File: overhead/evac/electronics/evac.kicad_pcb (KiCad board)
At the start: 2 copper layers, 145 x 47.3 mm, 39 parts, among them J1 Conn_02x01, J2 Conn_02x01, J3 Conn_02x03_Counter_Clockwise, J4 Conn_02x01

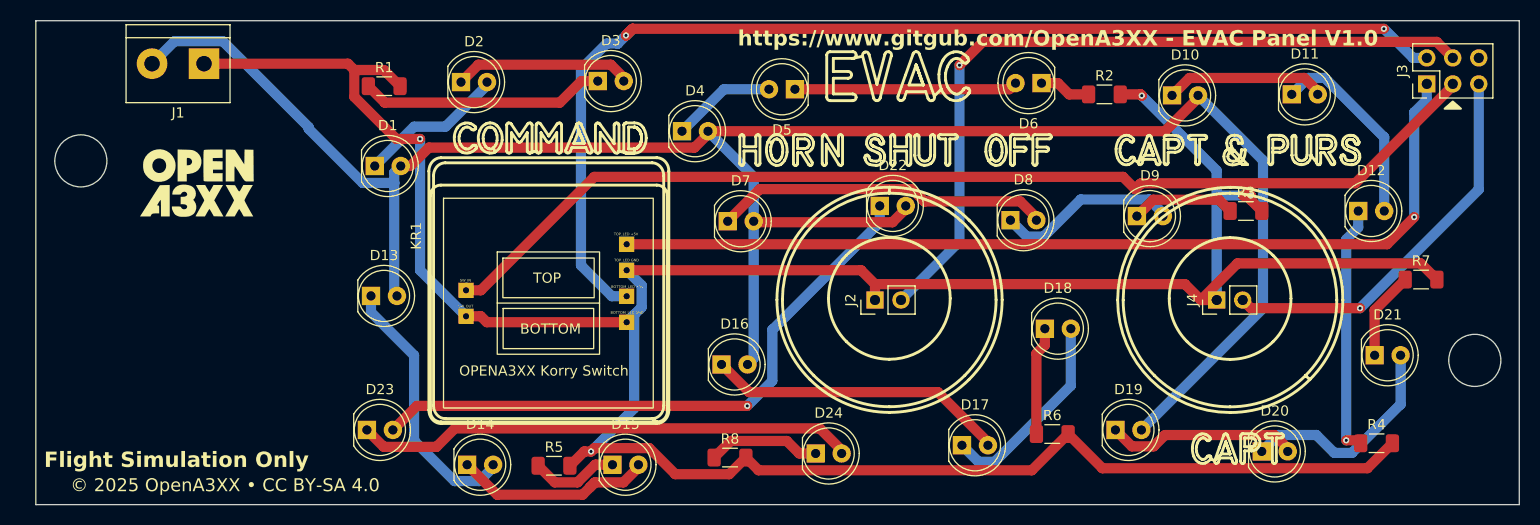
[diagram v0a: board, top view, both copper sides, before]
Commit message: Updated all LEDs for SMD!
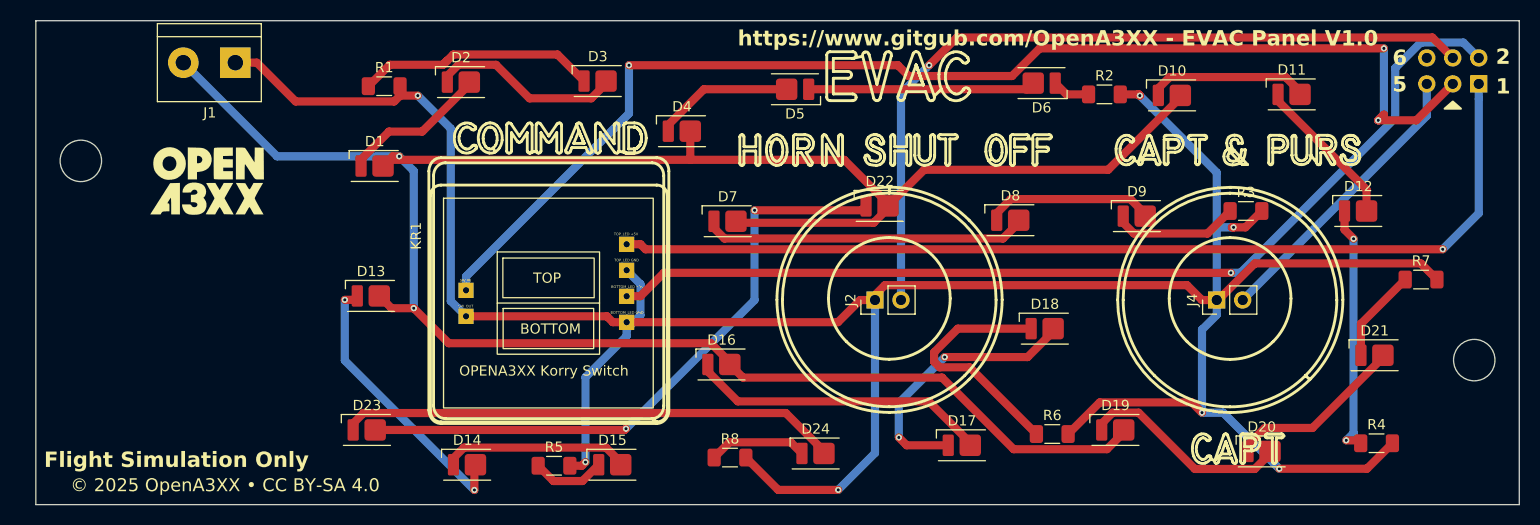
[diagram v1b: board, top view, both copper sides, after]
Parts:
- D1, D10, D11, D12, D13, D14, D15, D16, D17, D18, D19, D2, D20, D21, D22, D23, D24, D3, D4, D5, D6, D7, D8, D9: footprint LED_THT:LED_D5.0mm_Clear -> OpenA3XX:LED_Everlight-SMD3528_3.5x2.8mm_67-21ST
- J3: moved to B.Cu
- moved J3 5.08 mm to (213.6, 84.7)
- moved J1 3.06 mm to (92.1, 82.6)
- moved bottom 1.02 mm to (89.6, 94.1)
- moved top 1.02 mm to (89.4, 94.1)
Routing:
- net +12V: track 205.5 -> 225.6 mm, vias 0 -> 2
- net Net-(J3-Pin_2): track 114.1 -> 97.0 mm, vias 2 -> 1
- net Net-(J3-Pin_3): track 106.6 -> 123.1 mm, vias 0 -> 3
- net GND: track 294.3 -> 278.0 mm, vias 4 -> 7
- net Net-(D18-K): track 10.6 -> 24.3 mm
- net Net-(J3-Pin_5): track 38.5 -> 28.6 mm, vias 1 -> 0
- net Net-(D17-K): track 20.0 -> 26.8 mm, vias 0 -> 2
- net Net-(J3-Pin_1): track 91.6 -> 97.6 mm
- net Net-(D11-K): track 19.3 -> 15.0 mm
- net Net-(D20-K): track 21.7 -> 17.6 mm
- net Net-(D4-K): track 10.2 -> 13.6 mm
- net Net-(D9-K): track 10.2 -> 12.4 mm
- net Net-(J2-Pin_2): track 75.1 -> 77.2 mm
- net Net-(D19-K): track 18.8 -> 20.6 mm
- net Net-(D14-K): track 20.0 -> 18.3 mm
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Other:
- outline, holes or cut-outs redrawn
- board text added: "1"
- board text added: "2"
- board text added: "5"
- board text added: "6"

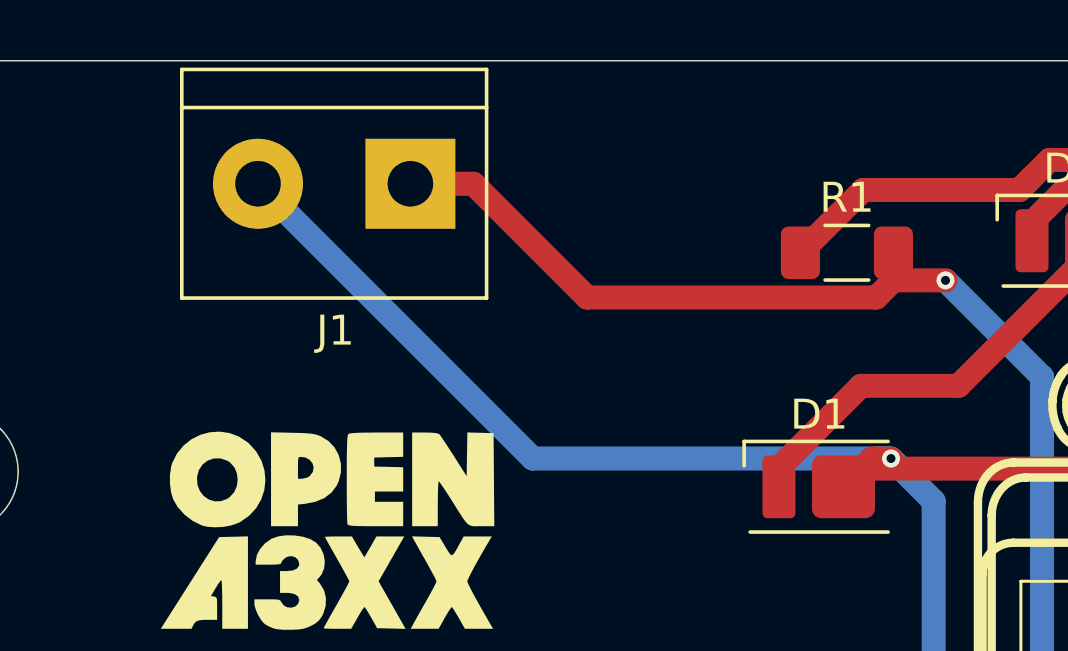
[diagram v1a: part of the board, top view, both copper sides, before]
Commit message: Added terminal connector to 3D models
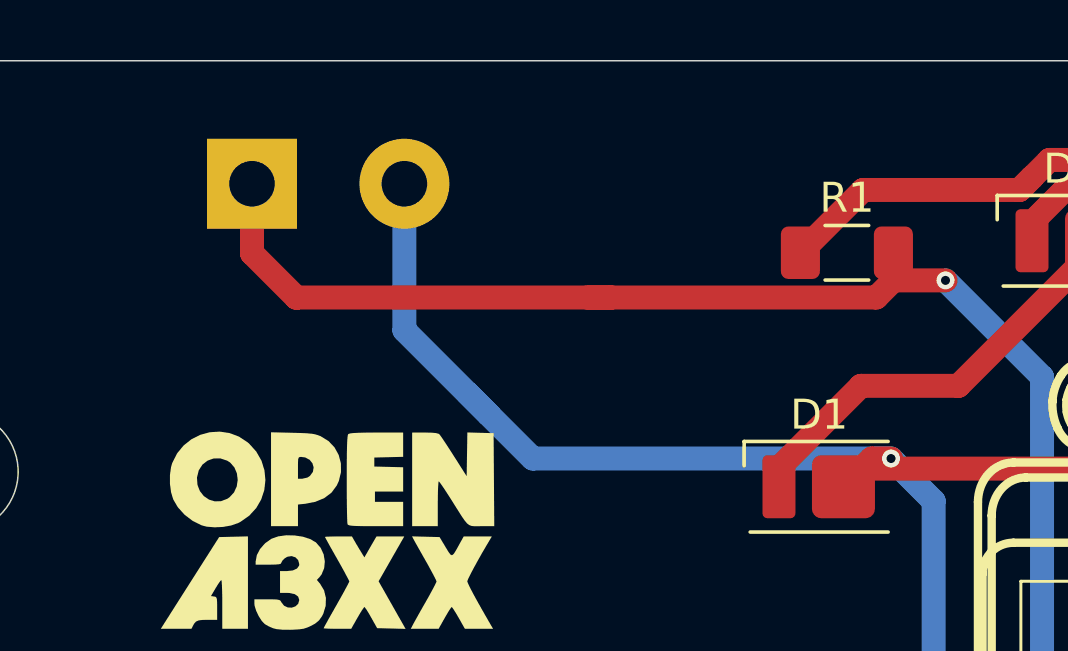
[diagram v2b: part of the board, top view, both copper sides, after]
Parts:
- J1: moved to B.Cu
- moved J1 5.28 mm to (86.8, 82.6), turned to 0 degrees
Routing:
- net GND: track 278.0 -> 285.4 mm
- net +12V: track 225.6 -> 227.5 mm
